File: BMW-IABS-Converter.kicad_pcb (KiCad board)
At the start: 2 copper layers, 61.4 x 49 mm, 57 parts, among them J1 SWD, J2 HCCPHPE24BKA90F, J3 GPIO_A0, J4 GPIO_A1, J5 GPIO_F0, J6 GPIO_F1, J7 GPIO_A2, J8 GND, Q1 IRLML0030TRPbF, Q2 IRLML0030TRPbF, Q4 IRFR9024, Q6 IRFR9024, U1 SN65HVD230, U2 STM32F042F4P6, U3 MC34063AD, U4 LM2904

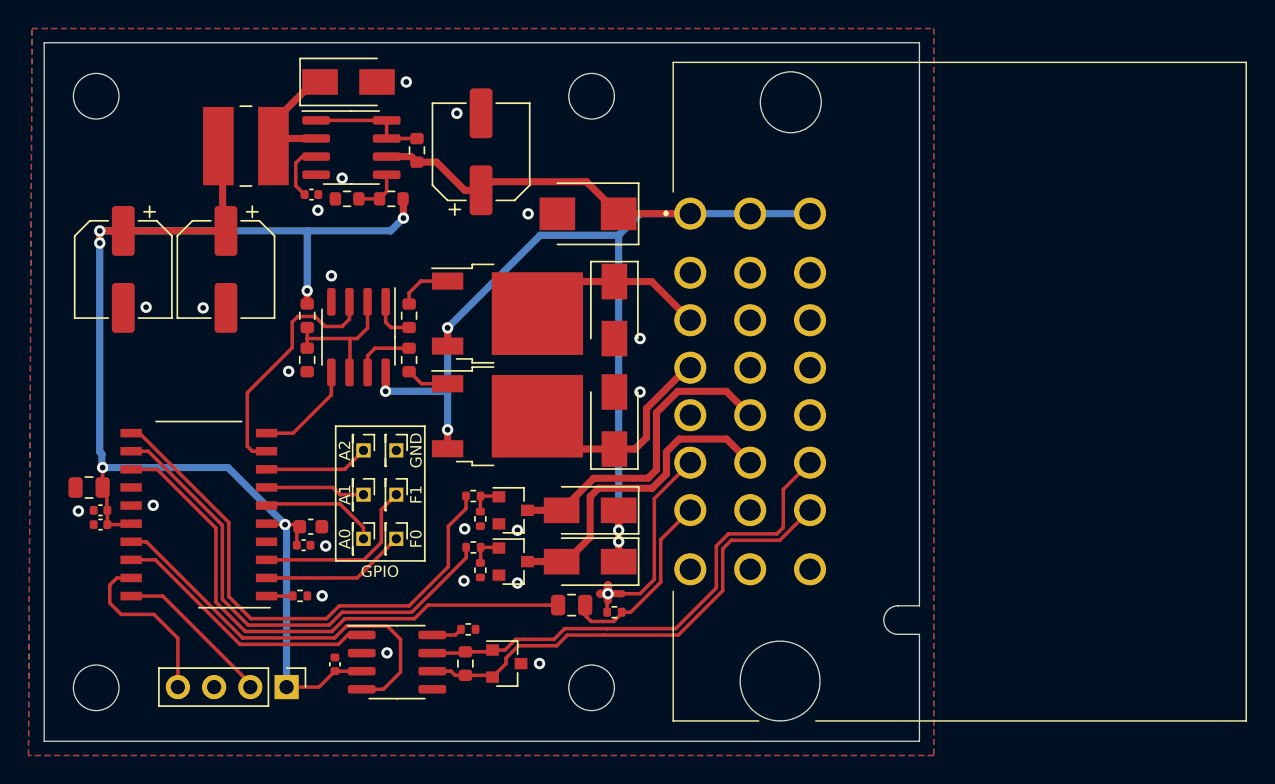
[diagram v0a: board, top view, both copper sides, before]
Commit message: Updated schematic and layout
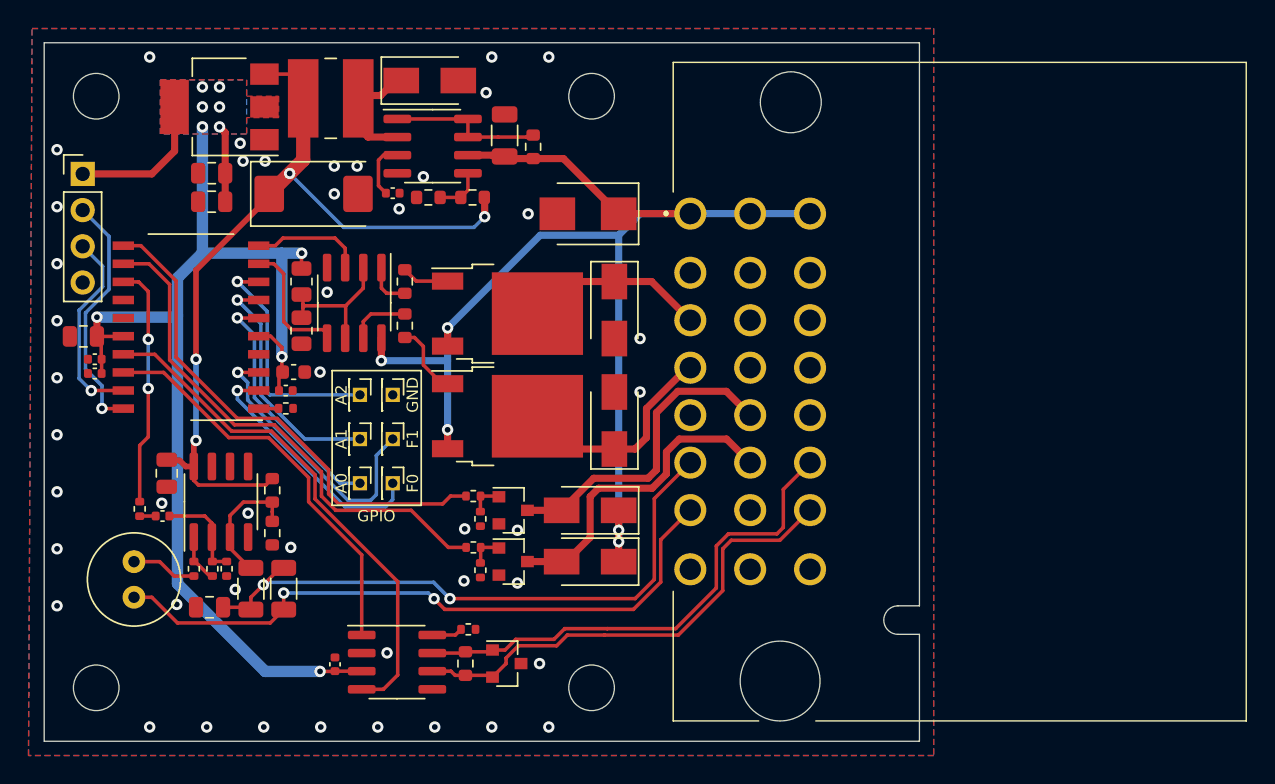
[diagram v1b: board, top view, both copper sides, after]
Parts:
- removed the C5 at (131.1, 105.8)
- removed NT2: TA- Tie, NetTie:NetTie-2_SMD_Pad0.5mm
- removed the R17 at (167.1, 113.0)
- added C13: 220uF (TAJD227K006RNJ-AVX), Capacitor_Tantalum_SMD:CP_EIA-7343-31_Kemet-D, F.Cu at (146.0, 83.6)
- added C15: 4.7uF, Capacitor_SMD:C_0805_2012Metric, F.Cu at (135.7, 103.2)
- added C2: 100nF, Capacitor_SMD:C_0402_1005Metric, F.Cu at (130.7, 96.2)
- added C6: 10uF, Capacitor_SMD:C_0805_2012Metric, F.Cu at (138.7, 112.6)
- added C8: 47uF 25V, Capacitor_THT:C_Radial_D6.3mm_H11.0mm_P2.50mm, F.Cu at (133.4, 111.9)
- added R10: 20K, Resistor_SMD:R_0603_1608Metric, F.Cu at (143.1, 107.4)
- added R11: 2K, Resistor_SMD:R_1206_3216Metric, F.Cu at (143.9, 111.3)
- added R12: 100R, Resistor_SMD:R_0402_1005Metric, F.Cu at (137.6, 109.9)
- added R14: 10K, Resistor_SMD:R_0402_1005Metric, F.Cu at (133.8, 105.7)
- added R15: 10K 1%, Resistor_SMD:R_0402_1005Metric, F.Cu at (138.9, 109.9)
- added R16: 10K 1% (NC), Resistor_SMD:R_0402_1005Metric, F.Cu at (139.9, 109.9)
- added R8: 20K, Resistor_SMD:R_0603_1608Metric, F.Cu at (143.1, 104.4)
- added R9: 10K, Resistor_SMD:R_1206_3216Metric, F.Cu at (141.6, 111.3)
- added U3: LMC662AIM, Package_SO:SOIC-8_3.9x4.9mm_P1.27mm, F.Cu at (139.5, 105.2)
- added U5: AMS1117-3.3, Package_TO_SOT_SMD:SOT-223-3_TabPin2, F.Cu at (139.4, 77.5)
- C10: value 330uF (EZV331M0JRC8) -> 4.7uF; footprint Capacitor_SMD:CP_Elec_6.3x7.7 -> Capacitor_SMD:C_0805_2012Metric
- C11: value 1uF -> 4.7uF
- C12: renamed from C2; value 220uF (EZV221M16RC8) -> 10uF; footprint Capacitor_SMD:CP_Elec_6.3x7.7 -> Capacitor_SMD:C_1206_3216Metric
- C9: value 330uF (EZV331M0JRC8) -> 100nF; footprint Capacitor_SMD:CP_Elec_6.3x7.7 -> Capacitor_SMD:C_0402_1005Metric
- Q2: value IRLML0030TRPbF -> IRLML0060TRPbF
- Q3: renamed from Q1; value IRLML0030TRPbF -> IRLML0060TRPbF
- R19: renamed from R6; value 3.3K 1% -> 3K 1%
- R20: renamed from R11; footprint Resistor_SMD:R_0603_1608Metric -> Resistor_SMD:R_0805_2012Metric
- R21: renamed from R5; value 2K 1% -> 1K 1%
- R22: renamed from R12; footprint Resistor_SMD:R_0603_1608Metric -> Resistor_SMD:R_0805_2012Metric
- moved J1 38.7 mm to (129.8, 82.2), turned to 0 degrees
- moved C11 37.9 mm to (138.8, 84.2)
- moved C9 17.5 mm to (135.4, 106.2), turned to 180 degrees
- moved R2 13.2 mm to (144.1, 98.7)
- moved U2 13.2 mm to (137.4, 93.0)
- moved C3 11.6 mm to (130.7, 95.2)
- moved C4 10.9 mm to (144.1, 97.4)
- moved C5 10.9 mm to (144.6, 96.1)
- moved C1 10.6 mm to (129.8, 93.6)
- moved R18 8.15 mm to (161.4, 80.3)
- moved L1 6.83 mm to (147.2, 76.9)
- moved C10 6.82 mm to (138.8, 82.2), turned to 180 degrees
- moved C14 5.70 mm to (151.6, 83.5)
- moved D7 5.70 mm to (154.2, 75.7)
- moved R19 5.70 mm to (157.2, 83.8)
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- renumbered C6 to C14, C7 to C4, C8 to C5, C4 to C7, D7 to D1, D3 to D2, D4 to D3, D6 to D4, D1 to D6, D2 to D7, LOGO2 to LOGO1, LOGO1 to LOGO2, Q4 to Q1, Q6 to Q4, R13 to R1, R3 to R13, R1 to R17, R4 to R18, R8 to R3, R7 to R4, R10 to R5, R9 to R6, R14 to R7, U4 to U1, U1 to U4, U3 to U6
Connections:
- C11 pad 1: /TAS -> +3V3
- C11 pad 2: /SPEED_PWM -> GND
- C9 pad 1: +3V3 -> Net-(C9-Pad1)
- C9 pad 2: GND -> Net-(C9-Pad2)
- J1 pad 3: GND -> /SWDIO
- J1 pad 4: /SWDIO -> GND
- L1 pad 2: +3V3 -> +5V
- R19 pad 2: +3V3 -> +5V
- U2 pad 10: /TAIL_LIGHT -> /BRAKE_LIGHT
- U2 pad 9: /BRAKE_LIGHT -> /TAIL_LIGHT
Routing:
- net +5V: track 0.00 -> 60.9 mm, vias 0 -> 4
- net /TAS: track 13.3 -> 46.4 mm, vias 0 -> 2
- net /TA-: track 11.9 -> 43.8 mm, vias 0 -> 2
- net /SPEED_PWM: track 38.5 -> 17.0 mm, vias 0 -> 2
- net /GPIO_A1: track 7.01 -> 17.1 mm, vias 0 -> 1
- net /CAN_TX: track 18.9 -> 28.6 mm
- net /BRAKE_LIGHT: track 17.4 -> 7.94 mm
- net /GPIO_A2: track 7.35 -> 16.7 mm, vias 0 -> 1
- net /GPIO_A0: track 8.33 -> 17.5 mm, vias 0 -> 1
- net Net-(R10-Pad1): track 0.00 -> 9.03 mm
- net /CAN_RX: track 27.9 -> 36.3 mm
- net /GPIO_F1: track 12.3 -> 20.2 mm, vias 0 -> 1
- net /GPIO_F0: track 10.2 -> 17.5 mm, vias 0 -> 1
- net Net-(C9-Pad1): track 0.00 -> 6.90 mm
- net /SWCLK: track 11.1 -> 17.3 mm, vias 0 -> 1
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- added copper zone on B.Cu, net +3V3
- added copper zone on F.Cu, net +3V3

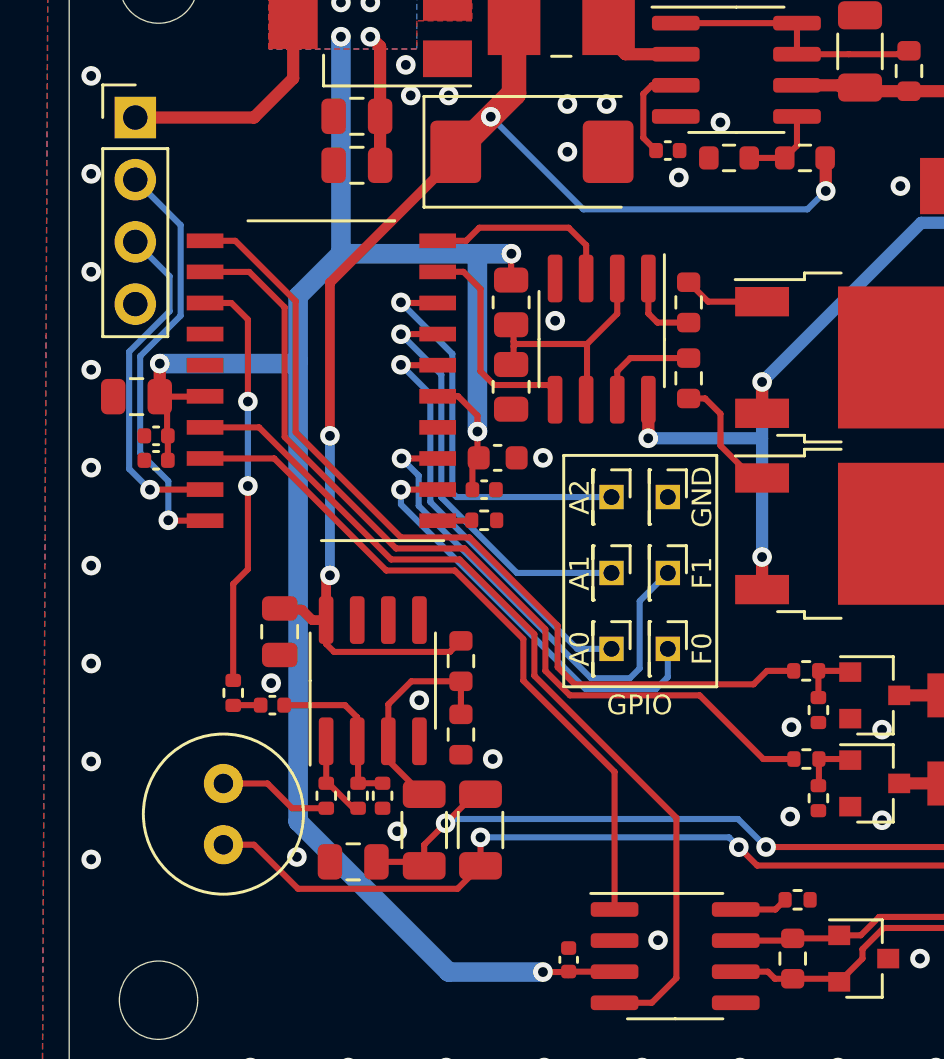
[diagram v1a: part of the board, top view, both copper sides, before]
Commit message: Fixed mcu package.
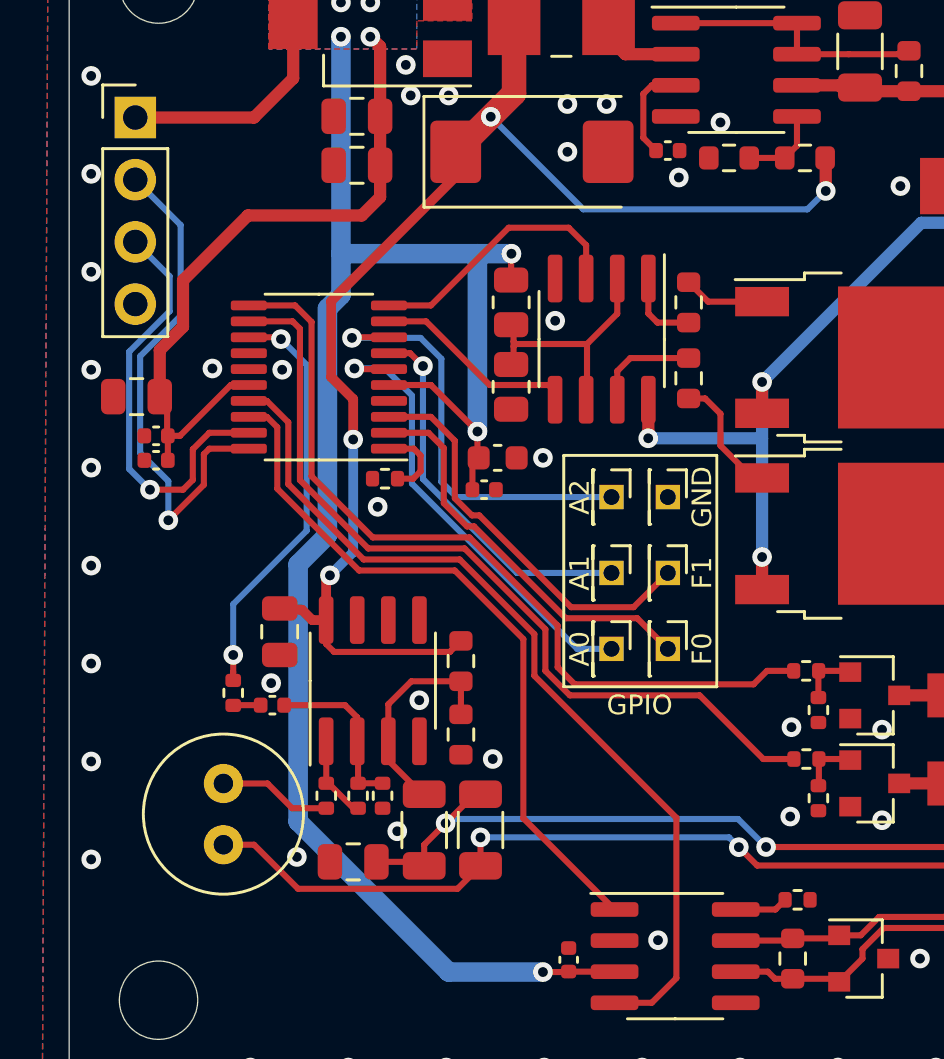
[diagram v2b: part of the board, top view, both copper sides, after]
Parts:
- U2: value STM32F042F4P6 -> STM32F042F4Px; footprint Package_SO:SO-20_12.8x7.5mm_P1.27mm -> Package_SO:TSSOP-20_4.4x6.5mm_P0.65mm
- moved LOGO2 6.91 mm to (144.4, 97.2)
- moved R2 4.39 mm to (140.0, 97.0), turned to 180 degrees
- moved U2 0.18 mm to (137.3, 92.8)
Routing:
- net +3V3: track 95.8 -> 108.7 mm, vias 10 -> 9
- net /SWCLK: track 17.3 -> 21.1 mm
- net /GPIO_F1: track 20.2 -> 16.6 mm, vias 1 -> 0
- net /SWDIO: track 14.0 -> 17.5 mm
- net /BRAKE_LIGHT: track 7.94 -> 11.0 mm
- net /ABS_WARN_RLY: track 35.9 -> 33.6 mm
- net /GEN_WARN: track 36.4 -> 34.3 mm
- net /GPIO_A1: track 17.1 -> 15.5 mm
- net /BOOT0: track 1.55 -> 3.12 mm
- net /GPIO_A0: track 17.5 -> 18.8 mm
- net /GPIO_F0: track 17.5 -> 16.4 mm, vias 1 -> 0
- net /GPIO_A2: track 16.7 -> 17.8 mm
- net /TAIL_LIGHT: track 9.12 -> 8.30 mm
- net +5V: track 60.9 -> 61.6 mm
- net GND: vias 45 -> 48
